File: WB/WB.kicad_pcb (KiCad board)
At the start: 2 copper layers, 80.9 x 90.2 mm, 34 parts, among them J1 Conn_01x04, J2 Conn_01x04, J3 Conn_01x04, J4 Screw_Terminal_01x02, Q1 Q_NMOS_GDS, Q2 Q_NMOS_GDS, Q3 Q_NMOS_GDS, Q4 Q_NMOS_GDS, Q5 Q_NMOS_GDS, Q6 Q_NPN_ECB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

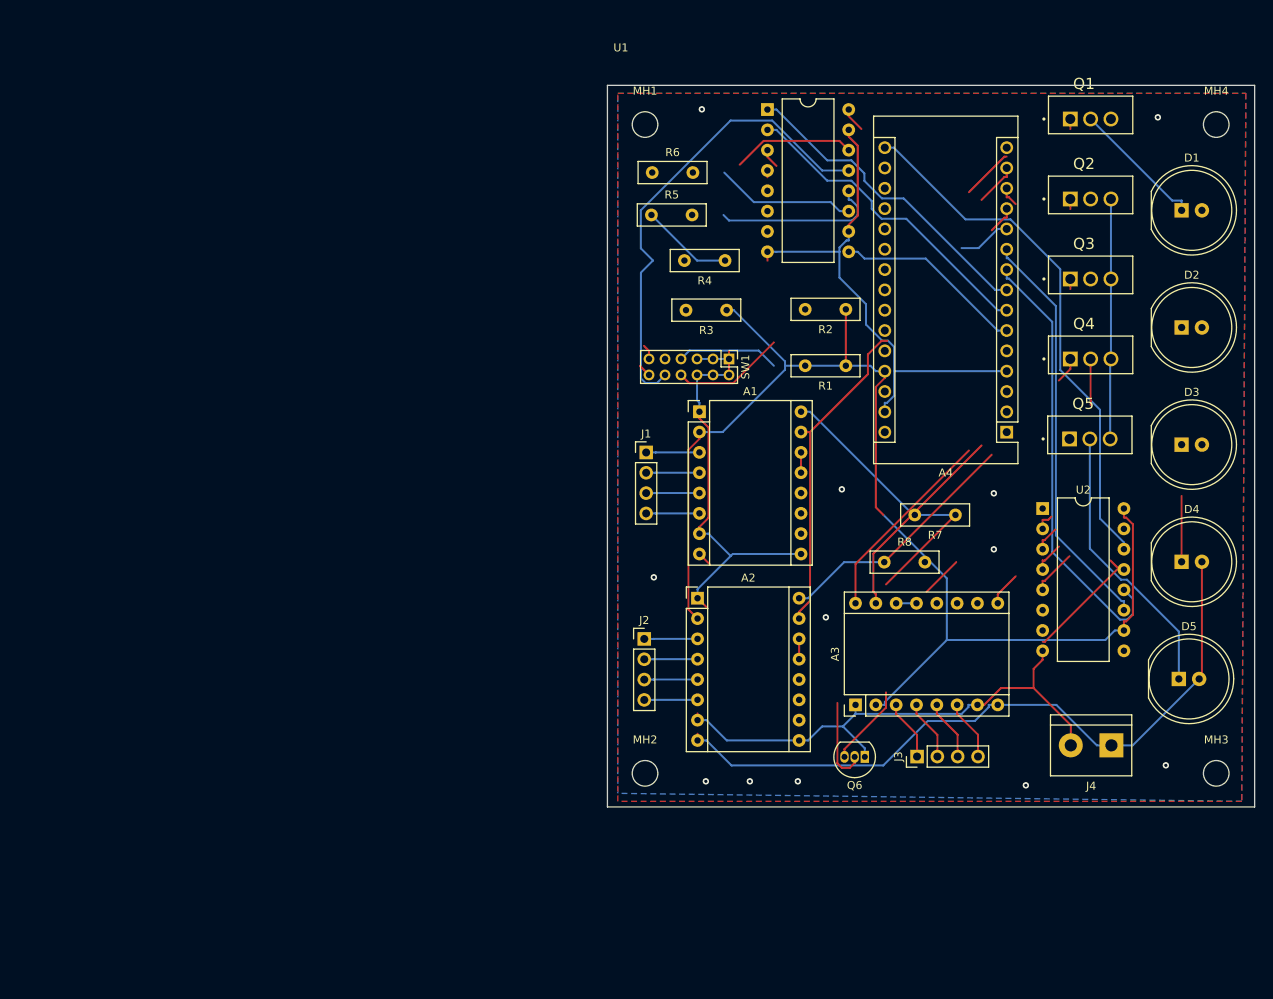
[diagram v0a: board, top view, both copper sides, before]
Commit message: ファン、アクチュエーターを追加。配置を修正
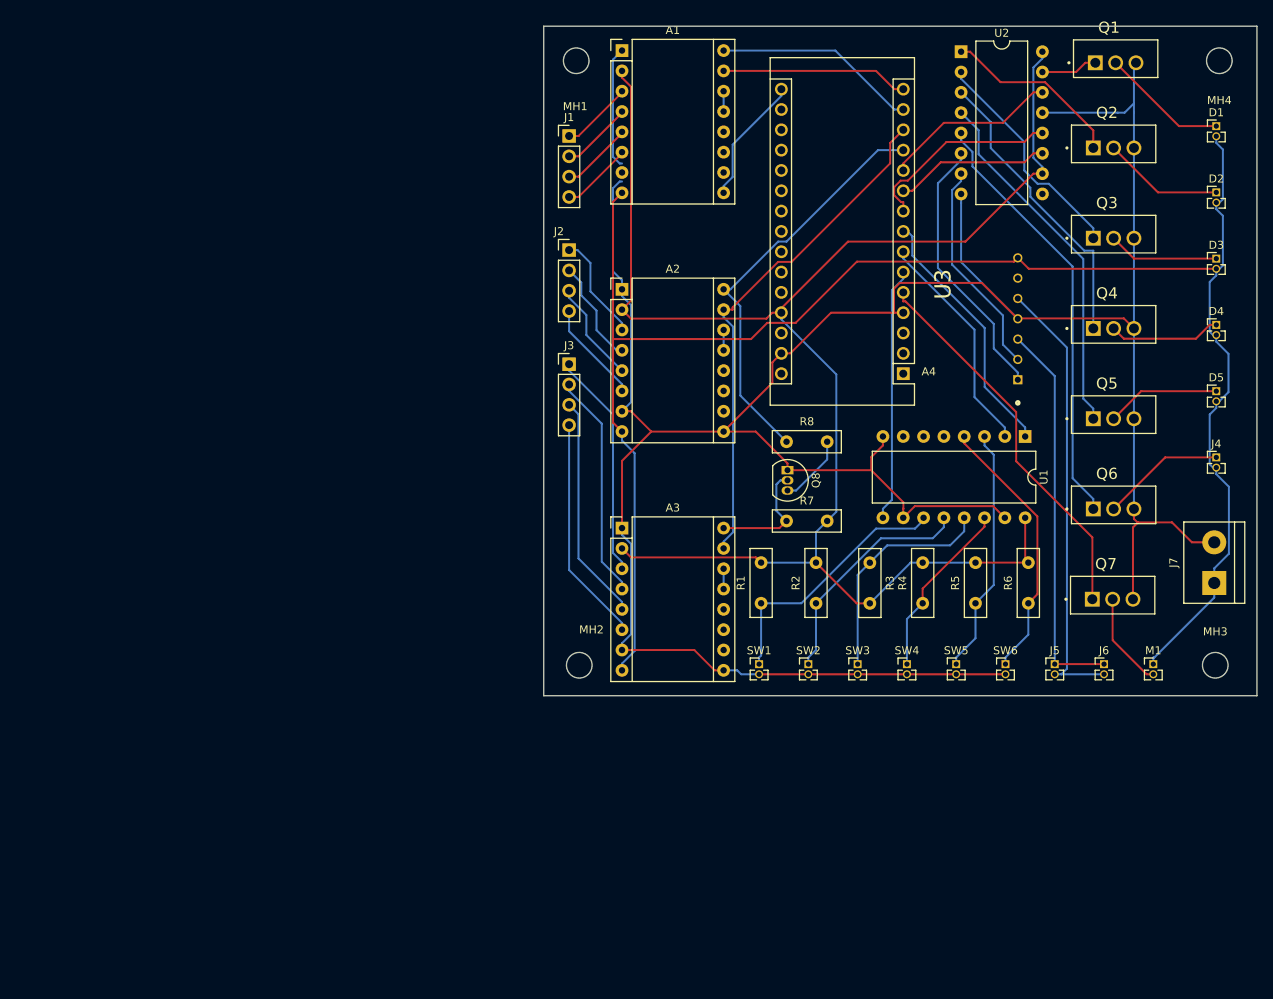
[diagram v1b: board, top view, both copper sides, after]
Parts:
- added J5: Actuator, Connector_PinHeader_1.27mm:PinHeader_1x02_P1.27mm_Vertical, F.Cu at (213.6, 102.3)
- added J6: Actuator, Connector_PinHeader_1.27mm:PinHeader_1x02_P1.27mm_Vertical, F.Cu at (219.8, 102.3)
- added J7: Screw_Terminal_01x02, TerminalBlock:TerminalBlock_bornier-2_P5.08mm, F.Cu at (233.6, 92.2)
- added M1: Fan, Connector_PinHeader_1.27mm:PinHeader_1x02_P1.27mm_Vertical, F.Cu at (225.9, 102.3)
- added Q7: Q_NMOS_GDS, 2sk2232:TO254P1054X470X1955-3, F.Cu at (220.9, 94.2)
- added Q8: Q_NPN_ECB, Package_TO_SOT_THT:TO-92_Inline, F.Cu at (180.2, 78.1)
- added SW2: SW_Push, Connector_PinHeader_1.27mm:PinHeader_1x02_P1.27mm_Vertical, F.Cu at (182.8, 102.3)
- added SW3: SW_Push, Connector_PinHeader_1.27mm:PinHeader_1x02_P1.27mm_Vertical, F.Cu at (189.0, 102.3)
- added SW4: SW_Push, Connector_PinHeader_1.27mm:PinHeader_1x02_P1.27mm_Vertical, F.Cu at (195.1, 102.3)
- added SW5: SW_Push, Connector_PinHeader_1.27mm:PinHeader_1x02_P1.27mm_Vertical, F.Cu at (201.3, 102.3)
- added SW6: SW_Push, Connector_PinHeader_1.27mm:PinHeader_1x02_P1.27mm_Vertical, F.Cu at (207.5, 102.3)
- added U3: TB6643KQ, TB6643KQ:SIP1005W50P254L1965H1265Q7, F.Cu at (206.5, 59.2)
- D1, D2, D3, D4, D5: footprint LED_THT:LED_D10.0mm -> Connector_PinHeader_1.27mm:PinHeader_1x02_P1.27mm_Vertical
- J4: value Screw_Terminal_01x02 -> Pump; footprint TerminalBlock:TerminalBlock_bornier-2_P5.08mm -> Connector_PinHeader_1.27mm:PinHeader_1x02_P1.27mm_Vertical
- Q1, Q2, Q3, Q4, Q5: footprint 2k2232:TO254P1054X470X1955-3 -> 2sk2232:TO254P1054X470X1955-3
- Q6: value Q_NPN_ECB -> Q_NMOS_GDS; footprint Package_TO_SOT_THT:TO-92_Inline -> 2sk2232:TO254P1054X470X1955-3
- R2, R3, R4, R5, R6: value R -> z
- SW1: value SW_DIP_x06 -> SW_Push; footprint Connector_PinHeader_2.00mm:PinHeader_2x06_P2.00mm_Vertical -> Connector_PinHeader_1.27mm:PinHeader_1x02_P1.27mm_Vertical
- moved R6 71.5 mm to (210.3, 94.7), turned to 90 degrees
- moved J3 65.6 mm to (152.9, 64.9), turned to 0 degrees
- moved R5 63.2 mm to (203.7, 94.7), turned to 90 degrees
- moved U2 58.0 mm to (201.9, 25.8)
- moved U1 52.0 mm to (209.9, 73.9), turned to -90 degrees
- moved J2 49.5 mm to (152.9, 50.6)
- moved R4 49.5 mm to (197.1, 94.7), turned to 90 degrees
- moved A1 46.2 mm to (159.5, 25.7)
- moved Q6 43.9 mm to (221.0, 83.0), turned to 0 degrees
- moved J1 40.7 mm to (152.9, 36.3)
- moved A2 39.7 mm to (159.5, 55.5)
- moved SW1 38.3 mm to (176.7, 102.3), turned to 0 degrees
- moved J4 38.3 mm to (233.8, 76.5), turned to 0 degrees
- moved R2 36.9 mm to (183.8, 94.7), turned to 90 degrees
- moved A3 36.6 mm to (159.5, 85.3), turned to 0 degrees
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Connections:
- A1 pad 9: GND -> Net-(A1-Pad9)
- A2 pad 15: Net-(A1-Pad15) -> Net-(A2-Pad15)
- A3 pad 15: Net-(A3-Pad15) -> Net-(A2-Pad15)
- A3 pad 9: Net-(A3-Pad9) -> GND
- A4 pad 11: Net-(A1-Pad15) -> Net-(A4-Pad11)
- A4 pad 13: Net-(A3-Pad9) -> Net-(A2-Pad15)
- A4 pad 14: Net-(A3-Pad15) -> Net-(A1-Pad16)
- A4 pad 15: Net-(A3-Pad16) -> Net-(A1-Pad15)
- A4 pad 16: Net-(A4-Pad16) -> Net-(A1-Pad9)
- A4 pad 5: unconnected-(A4-Pad5) -> Net-(A4-Pad5)
- J4 pad 1: +24V -> Net-(Q6-Pad2)
- J4 pad 2: GND -> +24V
- Q6 pad 1: GND -> Net-(Q6-Pad1)
- Q6 pad 2: Net-(A1-Pad16) -> Net-(Q6-Pad2)
- Q6 pad 3: Net-(Q6-Pad3) -> GND
- R1 pad 1: VCC -> D0
- R1 pad 2: Net-(R1-Pad2) -> VCC
- R2 pad 1: VCC -> D1
- R2 pad 2: Net-(R2-Pad2) -> VCC
- R3 pad 1: VCC -> D2
- R3 pad 2: Net-(R3-Pad2) -> VCC
- R4 pad 1: VCC -> D3
- R4 pad 2: Net-(R4-Pad2) -> VCC
- R5 pad 1: VCC -> D4
- R5 pad 2: Net-(R5-Pad2) -> VCC
- R6 pad 1: VCC -> D5
- R6 pad 2: Net-(R6-Pad2) -> VCC
- R7 pad 1: Net-(A1-Pad16) -> Net-(A3-Pad16)
- R8 pad 2: Net-(Q6-Pad3) -> Net-(Q8-Pad3)
- SW1 pad 1: GND -> D0
- U1 pad 11: Net-(R6-Pad2) -> D0
- U1 pad 12: Net-(R5-Pad2) -> D1
- U1 pad 13: Net-(R4-Pad2) -> D2
- U1 pad 14: Net-(R3-Pad2) -> D3
- U1 pad 3: Net-(R2-Pad2) -> D4
- U1 pad 4: Net-(R1-Pad2) -> D5
- U2 pad 1: Net-(Q1-Pad1) -> Net-(Q2-Pad1)
- U2 pad 14: Net-(A4-Pad16) -> Net-(A4-Pad11)
- U2 pad 15: unconnected-(U2-Pad15) -> Net-(Q1-Pad1)
- U2 pad 2: Net-(Q2-Pad1) -> Net-(Q3-Pad1)
- U2 pad 3: Net-(Q3-Pad1) -> Net-(Q4-Pad1)
- U2 pad 4: Net-(Q4-Pad1) -> Net-(Q5-Pad1)
- U2 pad 5: Net-(Q5-Pad1) -> Net-(Q6-Pad1)
- U2 pad 6: unconnected-(U2-Pad6) -> Net-(U2-Pad6)
- U2 pad 7: unconnected-(U2-Pad7) -> Net-(U2-Pad7)
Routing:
- net GND: track 231.9 -> 360.5 mm
- net +24V: track 90.4 -> 218.6 mm
- net Net-(A1-Pad16): track 104.8 -> 25.5 mm
- net Net-(A4-Pad16): track 66.5 -> 0.00 mm
- net Net-(A2-Pad15): track 0.00 -> 64.3 mm
- net Net-(R4-Pad2): track 59.2 -> 0.00 mm
- net Net-(J5-Pad2): track 0.00 -> 56.0 mm
- net Net-(Q6-Pad1): track 0.00 -> 53.8 mm
- net Net-(J5-Pad1): track 0.00 -> 48.7 mm
- net Net-(A4-Pad5): track 0.00 -> 48.3 mm
- net Net-(Q5-Pad1): track 5.76 -> 45.1 mm
- net D5: track 0.00 -> 33.9 mm
- net Net-(U2-Pad6): track 0.00 -> 33.6 mm
- net D0: track 0.00 -> 32.6 mm
- net Net-(A4-Pad10): track 51.4 -> 19.3 mm
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- removed copper zone on B.Cu, net GND
- removed copper zone on F.Cu, net GND
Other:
- board size 80.9 x 90.2 mm -> 89.2 x 83.7 mm
- board text added: "AutoEraser"

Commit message: 配線の修正
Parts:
- added J2: Conn_01x04, Connector_PinHeader_2.54mm:PinHeader_1x04_P2.54mm_Vertical, F.Cu at (153.3, 53.5)
- moved J4 22.9 mm to (153.3, 87.8)
- moved J3 20.0 mm to (153.3, 70.6)
- moved D1 0.76 mm to (234.6, 35.0)
- moved D3 0.76 mm to (234.6, 51.6)
- moved D4 0.76 mm to (234.6, 59.9)
- moved D2 0.76 mm to (234.6, 43.3)
- moved D5 0.76 mm to (234.6, 68.2)
- moved J5 0.76 mm to (234.6, 76.4)
- moved J1 0.38 mm to (153.3, 36.3)
- renumbered J2 to J3, J3 to J4, J4 to J5, J5 to J6, J6 to J7, J7 to J8
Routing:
- net Net-(A3-Pad6): track 28.3 -> 7.71 mm
- net Net-(A3-Pad5): track 28.3 -> 7.71 mm
- net Net-(A3-Pad4): track 28.3 -> 7.71 mm
- net Net-(A3-Pad3): track 28.3 -> 7.72 mm
- net Net-(A1-Pad4): track 9.03 -> 28.1 mm
- net Net-(A1-Pad3): track 9.03 -> 27.5 mm
- net Net-(A1-Pad5): track 9.03 -> 27.5 mm
- net Net-(A1-Pad6): track 9.03 -> 27.1 mm
- net GND: track 360.5 -> 366.1 mm
- net Net-(Q4-Pad1): track 37.0 -> 41.9 mm
- net D3: track 22.3 -> 25.1 mm
- net +24V: track 218.6 -> 220.7 mm
- net Net-(D5-Pad1): track 14.3 -> 16.1 mm
- net Net-(D4-Pad1): track 14.1 -> 15.8 mm
- net Net-(Q2-Pad1): track 22.8 -> 23.9 mm
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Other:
- board text added: "Made by Ruchi"

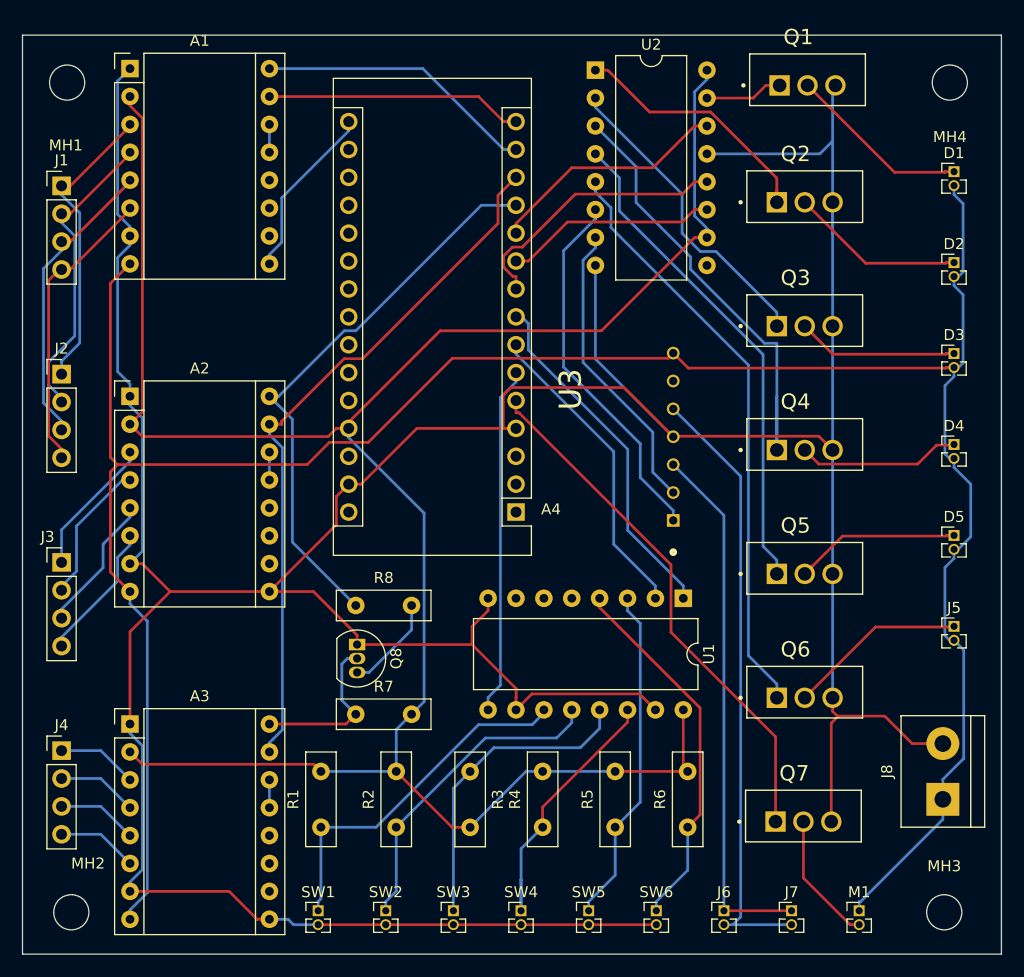
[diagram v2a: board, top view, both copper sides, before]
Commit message: ICのDIPを変更。
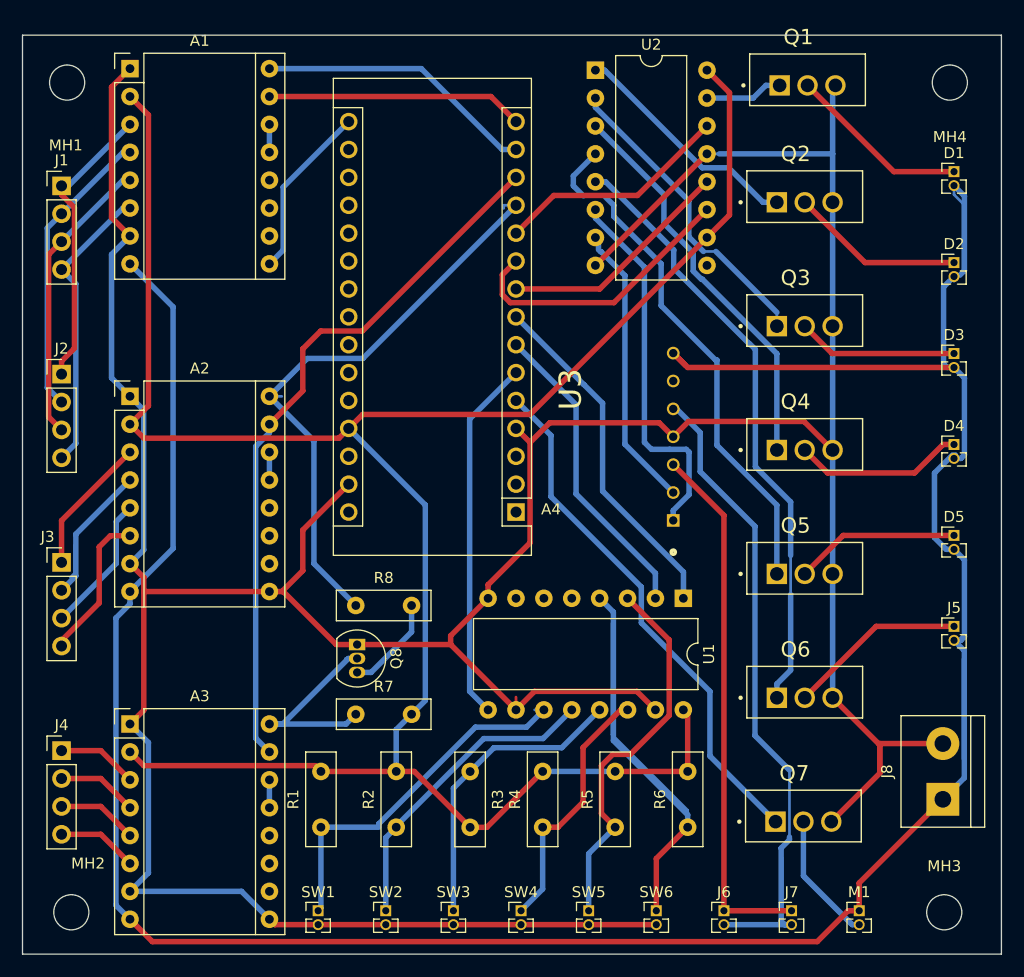
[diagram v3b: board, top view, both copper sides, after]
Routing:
- net GND: track 366.1 -> 414.3 mm
- net +24V: track 220.7 -> 259.7 mm
- net D5: track 34.3 -> 54.4 mm
- net Net-(J5-Pad2): track 56.0 -> 71.0 mm
- net Net-(M1-Pad2): track 12.0 -> 23.8 mm
- net Net-(A4-Pad7): track 28.4 -> 40.2 mm
- net Net-(A3-Pad16): track 14.9 -> 24.8 mm
- net Net-(A4-Pad10): track 19.3 -> 26.0 mm
- net Net-(A2-Pad16): track 52.0 -> 57.0 mm
- net Net-(D4-Pad1): track 15.8 -> 20.8 mm
- net D4: track 30.9 -> 35.0 mm
- net Net-(A4-Pad9): track 25.0 -> 21.4 mm
- net Net-(A2-Pad4): track 13.0 -> 15.7 mm
- net Net-(Q2-Pad1): track 23.9 -> 21.5 mm
- net Net-(Q5-Pad1): track 45.7 -> 48.0 mm
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
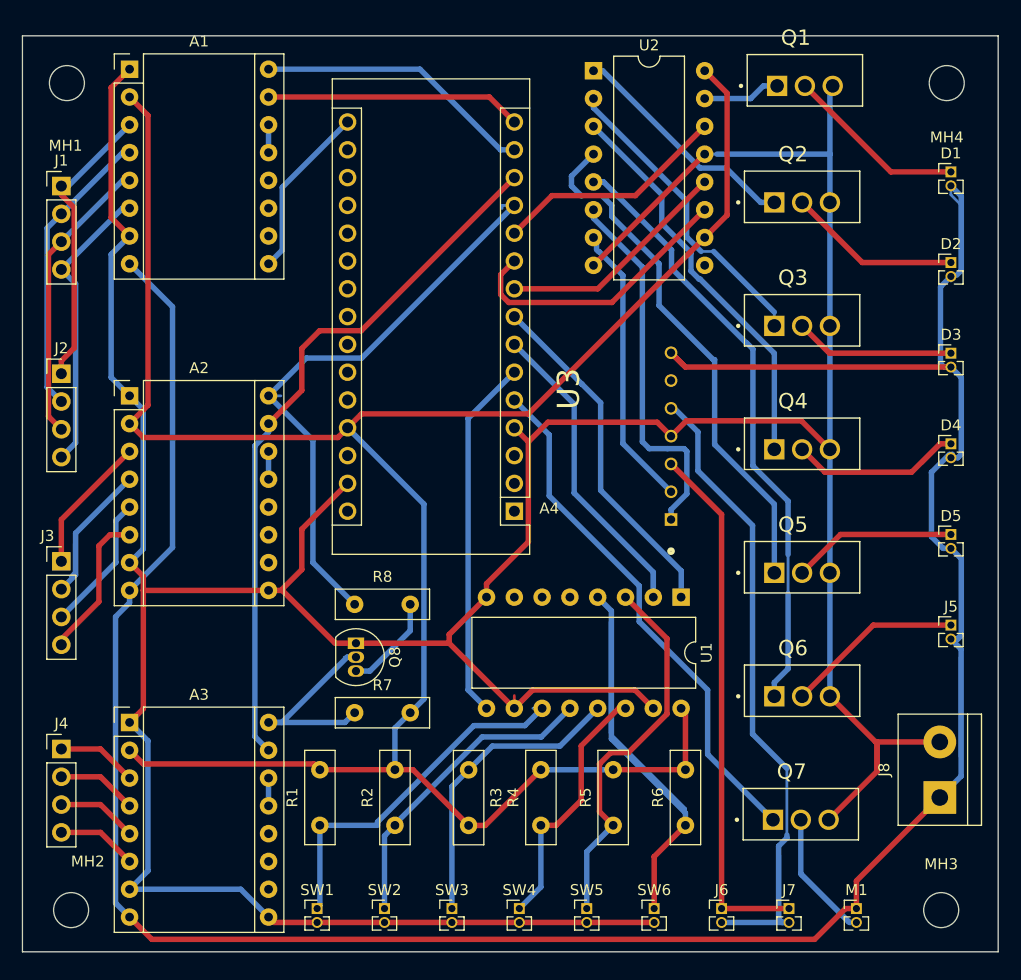
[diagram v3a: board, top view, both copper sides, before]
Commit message: 配線の太さを太く
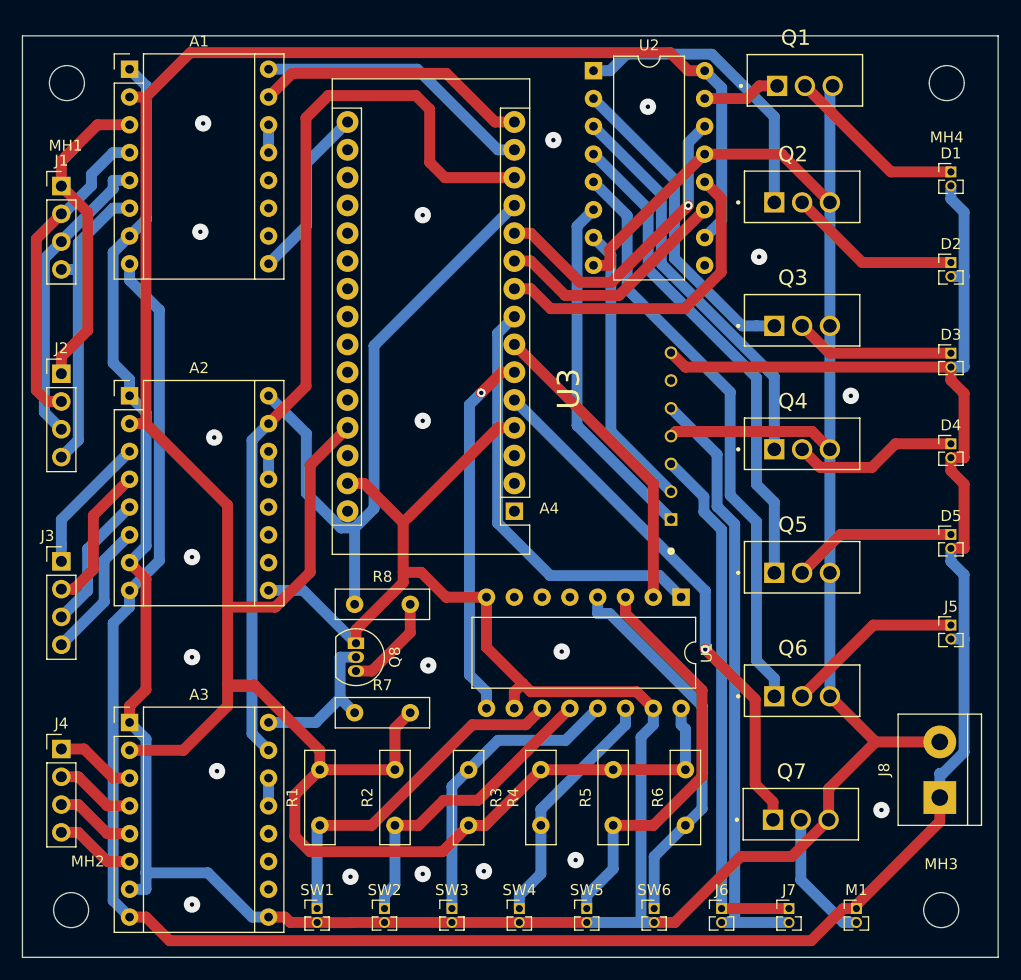
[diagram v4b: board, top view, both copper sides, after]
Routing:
- net GND: track 414.3 -> 366.6 mm
- net VCC: track 206.7 -> 245.7 mm
- net +24V: track 259.7 -> 236.1 mm
- net Net-(A2-Pad15): track 64.9 -> 86.3 mm
- net D5: track 54.4 -> 34.9 mm
- net Net-(J5-Pad2): track 71.0 -> 55.5 mm
- net Net-(A4-Pad7): track 40.2 -> 28.4 mm
- net Net-(M1-Pad2): track 23.8 -> 12.2 mm
- net Net-(A3-Pad16): track 24.8 -> 14.5 mm
- net Net-(A4-Pad9): track 21.4 -> 29.9 mm
- net Net-(A4-Pad8): track 32.0 -> 39.1 mm
- net Net-(A4-Pad11): track 21.4 -> 28.5 mm, vias 0 -> 1
- net Net-(Q4-Pad1): track 42.6 -> 36.4 mm
- net Net-(Q2-Pad1): track 21.5 -> 27.3 mm
- net Net-(D4-Pad1): track 20.8 -> 15.2 mm
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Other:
- board size 89.2 x 83.7 mm -> 89.2 x 84.2 mm
